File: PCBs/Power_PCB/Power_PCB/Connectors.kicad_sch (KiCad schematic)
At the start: 15 parts, among them J11 Conn_01x04, J13 Conn_01x04, J14 Conn_01x04, J16 Conn_01x02, J17 Conn_01x02, J19 Conn_01x02, J20 Conn_01x02, J4 Conn_01x02, J5 Conn_01x02, J6 Conn_01x02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

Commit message: Second iteration power board
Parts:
- removed J16, J17, J19, J20: Conn_01x02, TerminalBlock:TerminalBlock_Altech_AK300-2_P5.00mm, symbol Connector_Generic:Conn_01x02
- added J15, J16, J17, J9: 8PCV-02-006, 8PCV02006, symbol 8PCV-02-006:8PCV-02-006
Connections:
- net 14V8_ARM_OUT: now also J9.2
- net 14V8_COMMS_OUT: now also J16.2
- net 14V8_DRILL_OUT: now also J17.2
- net 14V8_DRIVE_OUT: now also J15.2
- net GND: now also J15.1, J16.1, J17.1, J9.1

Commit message: Modified output connectors to female
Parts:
- J15, J16, J17, J9: footprint 8PCV02006 -> iprl_footprints:8PCV02006
- J4, J5, J6, J8: footprint Connector_AMASS:AMASS_XT60PW-M_1x02_P7.20mm_Horizontal -> Connector_AMASS:AMASS_XT60PW-F_1x02_P7.20mm_Horizontal
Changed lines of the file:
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@@
 			)
 		)
-		(property "Footprint" "8PCV02006"
+		(property "Footprint" "iprl_footprints:8PCV02006"
 			(at 157.48 182.55 0)
 			(effects
@@
 			)
 		)
-		(property "Footprint" "8PCV02006"
+		(property "Footprint" "iprl_footprints:8PCV02006"
 			(at 200.66 162.23 0)
 			(effects
@@
 			)
 		)
-		(property "Footprint" "Connector_AMASS:AMASS_XT60PW-M_1x02_P7.20mm_Horizontal"
+		(property "Footprint" "Connector_AMASS:AMASS_XT60PW-F_1x02_P7.20mm_Horizontal"
 			(at 146.05 80.01 0)
 			(effects
@@
 			)
 		)
-		(property "Footprint" "Connector_AMASS:AMASS_XT60PW-M_1x02_P7.20mm_Horizontal"
+		(property "Footprint" "Connector_AMASS:AMASS_XT60PW-F_1x02_P7.20mm_Horizontal"
 			(at 189.23 59.69 0)
 			(effects
@@
 			)
 		)
-		(property "Footprint" "Connector_AMASS:AMASS_XT60PW-M_1x02_P7.20mm_Horizontal"
+		(property "Footprint" "Connector_AMASS:AMASS_XT60PW-F_1x02_P7.20mm_Horizontal"
 			(at 189.23 80.01 0)
 			(effects
@@
 			)
 		)
-		(property "Footprint" "Connector_AMASS:AMASS_XT60PW-M_1x02_P7.20mm_Horizontal"
+		(property "Footprint" "Connector_AMASS:AMASS_XT60PW-F_1x02_P7.20mm_Horizontal"
 			(at 146.05 59.69 0)
 			(effects
@@
 			)
 		)
-		(property "Footprint" "8PCV02006"
+		(property "Footprint" "iprl_footprints:8PCV02006"
 			(at 157.48 162.23 0)
 			(effects
@@
 			)
 		)
-		(property "Footprint" "8PCV02006"
+		(property "Footprint" "iprl_footprints:8PCV02006"
 			(at 200.66 182.55 0)
 			(effects

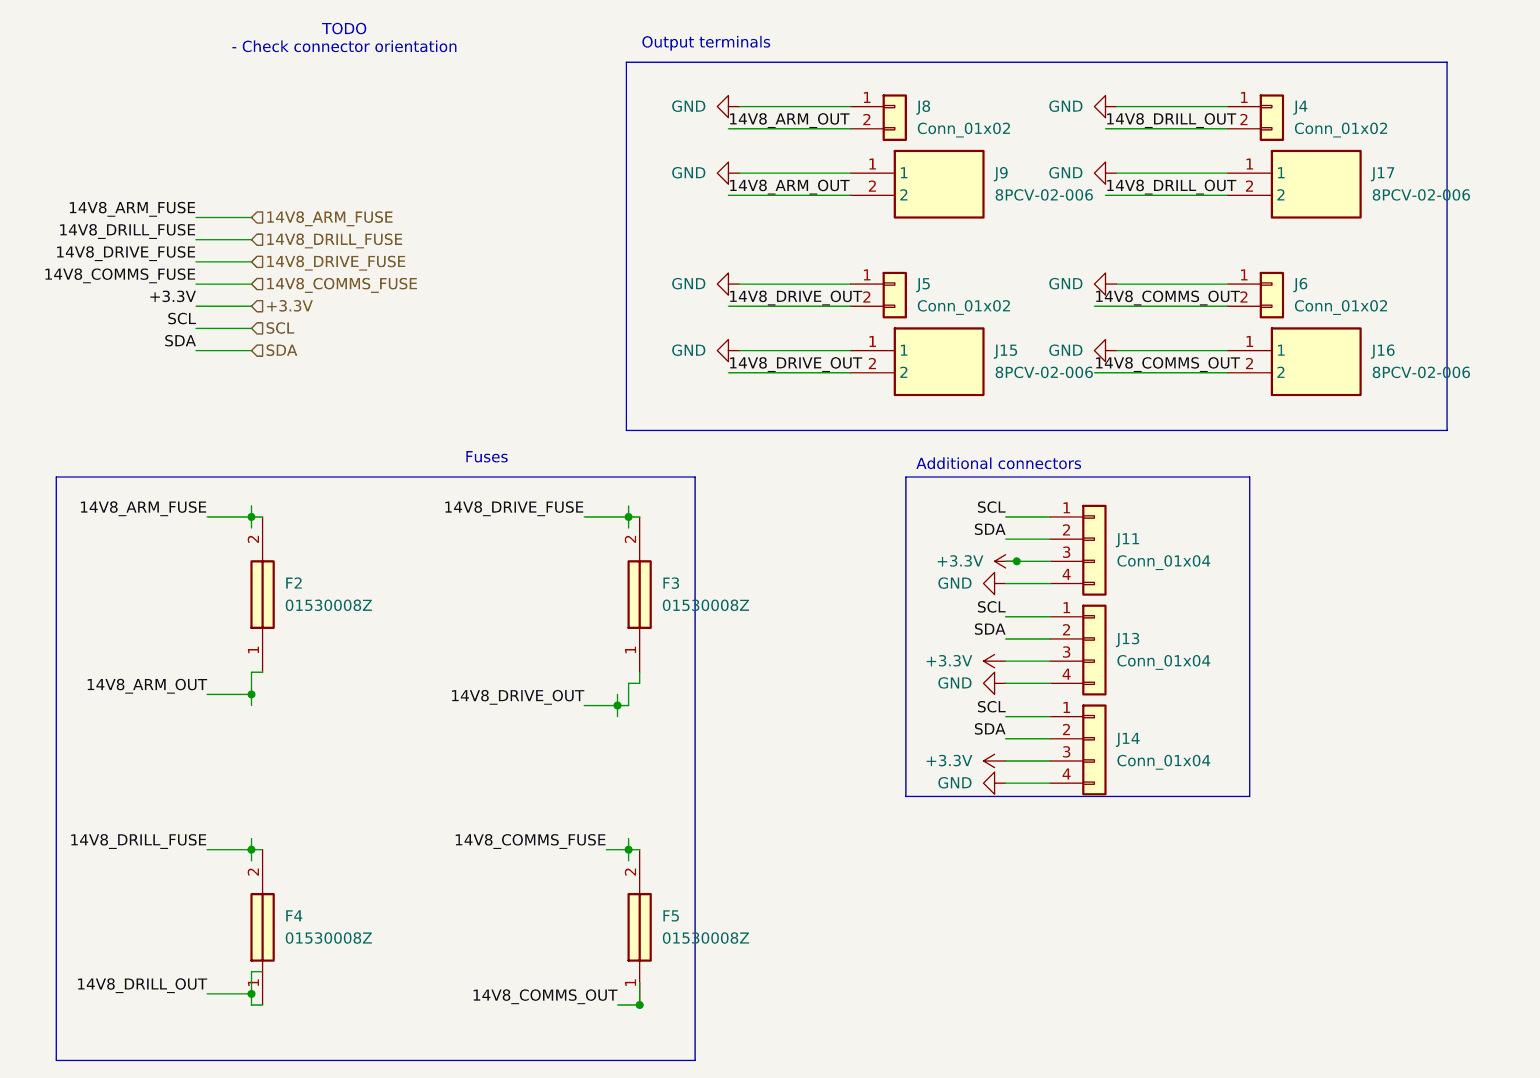
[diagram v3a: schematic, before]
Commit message: Replaced fuse holders with 01000064Z
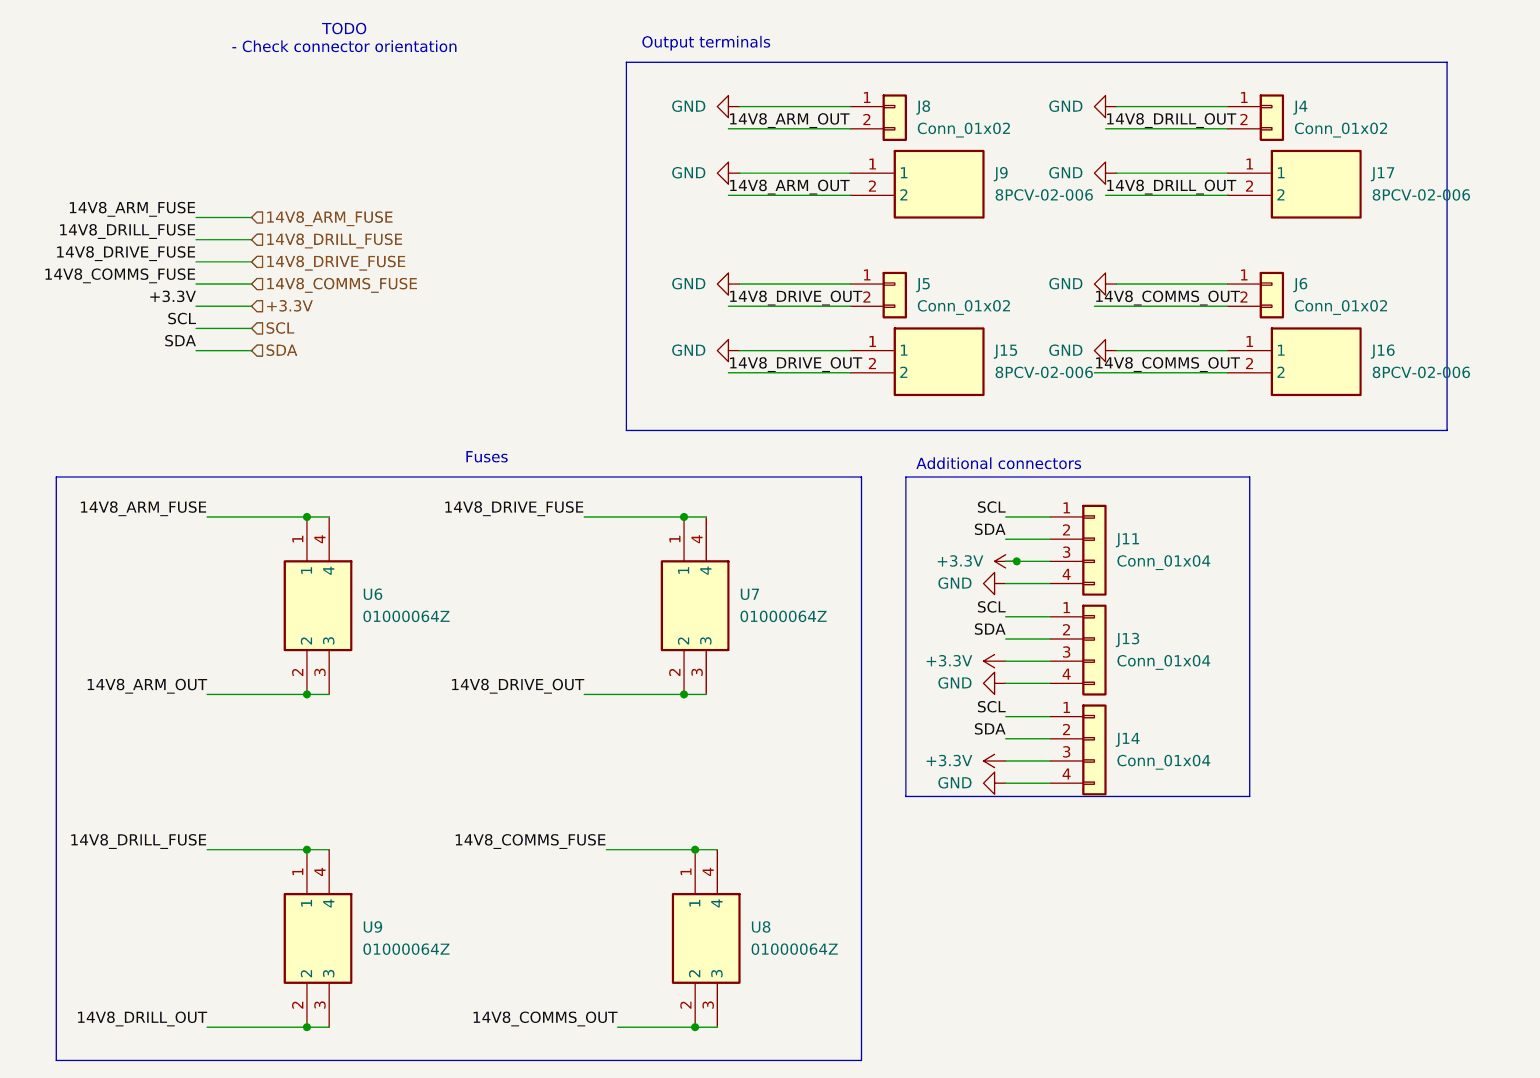
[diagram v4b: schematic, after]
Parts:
- removed F2, F3, F4, F5: 01530008Z, iprl_footprints:01530008, symbol 01530008Z:01530008Z
- added U6, U7, U8, U9: 01000064Z, 01000064Z, symbol 01000064Z:01000064Z
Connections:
- net 14V8_ARM_FUSE: now also U6.1, U6.4
- net 14V8_ARM_OUT: now also U6.2, U6.3
- net 14V8_COMMS_FUSE: now also U8.1, U8.4
- net 14V8_COMMS_OUT: now also U8.2, U8.3
- net 14V8_DRILL_FUSE: now also U9.1, U9.4
- net 14V8_DRILL_OUT: now also U9.2, U9.3
- net 14V8_DRIVE_FUSE: now also U7.1, U7.4
- net 14V8_DRIVE_OUT: now also U7.2, U7.3

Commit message: submitted power board
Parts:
- removed J15, J16, J17, J9: 8PCV-02-006, iprl_footprints:8PCV02006, symbol 8PCV-02-006:8PCV-02-006
- removed U6, U7, U8, U9: 01000064Z, 01000064Z, symbol 01000064Z:01000064Z
- added J15, J16, J17, J9: YK4420203000G, RHDR2W120P0X950_1X2_2050X1430X1790P, symbol YK4420203000G:YK4420203000G
- added U2, U6, U7, U8: 178.6164.0001, 178.6164.XXX1, symbol 178_6164_0001:178.6164.0001
- J11, J13, J14: footprint Connector_JST:JST_SH_BM04B-SRSS-TB_1x04-1MP_P1.00mm_Vertical -> Connector_JST:JST_PH_S4B-PH-K_1x04_P2.00mm_Horizontal
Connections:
- net 14V8_ARM_FUSE: now also U2.1
- net 14V8_ARM_OUT: now also J15.2, U2.2
- net 14V8_COMMS_FUSE: now also U8.1
- net 14V8_COMMS_OUT: now also J17.2, U8.2
- net 14V8_DRILL_FUSE: now also U6.1
- net 14V8_DRILL_OUT: now also J16.2, U6.2
- net 14V8_DRIVE_FUSE: now also U7.1
- net 14V8_DRIVE_OUT: now also J9.2, U7.2
- net GND: now also J15.1, J16.1, J17.1, J9.1
